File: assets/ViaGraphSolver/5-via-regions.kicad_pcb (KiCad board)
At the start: 2 copper layers, 0 parts

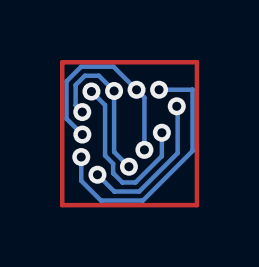
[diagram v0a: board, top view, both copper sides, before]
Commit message: ptimize via‑tile parsing with new SVG generation script to shrink 5‑region geometry and reach 98.7% solve rate
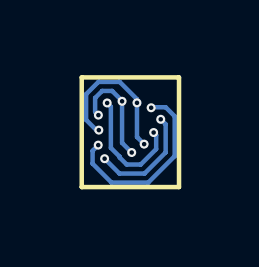
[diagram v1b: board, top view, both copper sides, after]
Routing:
- net net3: track 8.62 -> 6.30 mm
- net net5: track 6.96 -> 5.12 mm
- net net1: track 5.92 -> 4.11 mm
- net net4: track 5.34 -> 3.60 mm
- net net2: track 5.01 -> 3.70 mm
